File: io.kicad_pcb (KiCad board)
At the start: 2 copper layers, 182 x 139 mm, 37 parts, among them CON1 AVR_ISP, IC1 ATMEGA644P-P, J1 DB9, J2 DB9, P1 CONN_CTL_DATA, P2 CONN_ADDR, P3 SLOT1, P4 SLOT2, P5 SLOT3, P6 SLOT4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

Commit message: ugh
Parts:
- moved R2 18.3 mm to (115.7, 146.1)
- moved C11 7.62 mm to (70.0, 45.2)
- moved C12 7.62 mm to (51.3, 56.6)
- moved C9 7.62 mm to (51.3, 49.5)
- moved C10 7.62 mm to (70.0, 38.5)
- moved C8 7.62 mm to (51.3, 42.3)
- moved J2 7.62 mm to (95.6, 50.8)
- moved U6 7.62 mm to (57.1, 40.6)
- moved C2 6.60 mm to (150.8, 39.5)
- moved U1 6.60 mm to (158.8, 42.2)
- moved J1 3.81 mm to (84.7, 146.1)
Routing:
- net /A23: track 154.0 -> 219.4 mm
- net /RX: track 81.8 -> 41.2 mm
- net /TX: track 81.2 -> 41.6 mm
- net GND: track 513.9 -> 499.2 mm, vias 5 -> 4
- net /PAD_RIGHT: track 73.0 -> 59.4 mm
- net /PAD_SC: track 106.4 -> 94.2 mm
- net /A1: track 169.5 -> 181.5 mm
- net /PAD_LEFT: track 77.0 -> 65.3 mm
- net /A5: track 161.5 -> 173.1 mm
- net /PAD_AB: track 95.0 -> 85.3 mm
- net /PAD_DN: track 80.7 -> 71.0 mm
- net /A2: track 168.5 -> 177.5 mm
- net /~EN_S2: track 42.0 -> 33.2 mm
- net /A3: track 174.4 -> 183.1 mm
- net /A4: track 174.2 -> 182.5 mm
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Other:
- board size 182 x 139 mm -> 182 x 129 mm

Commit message: new layout
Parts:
- removed JP5: INT_S4, Pin_Headers:Pin_Header_Straight_2x01
- added R10: 4.7k, Resistors_SMD:R_0805, F.Cu at (20.8, 146.1)
- added R4: 4.7k, Resistors_SMD:R_0805, F.Cu at (20.8, 153.7)
- added R5: 4.7k, Resistors_SMD:R_0805, F.Cu at (37.1, 151.1)
- added R6: 4.7k, Resistors_SMD:R_0805, F.Cu at (20.8, 151.1)
- added R7: 4.7k, Resistors_SMD:R_0805, F.Cu at (37.0, 148.6)
- added R8: 4.7k, Resistors_SMD:R_0805, F.Cu at (20.8, 148.6)
- added R9: 4.7k, Resistors_SMD:R_0805, F.Cu at (37.0, 146.2)
- P6: value SLOT4 -> CONN_01X02; footprint m68kcomp1:edgecon_2x20 -> Pin_Headers:Pin_Header_Straight_1x02
- R1: moved to F.Cu
- R3: moved to B.Cu
- moved C2 221.0 mm to (-15.7, 184.7)
- moved C3 145.9 mm to (-5.00, 176.8)
- moved U1 130.6 mm to (38.1, 92.1), turned to 0 degrees
- moved P5 95.3 mm to (72.4, 73.7), turned to 90 degrees
- moved C4 91.1 mm to (36.4, 99.7), turned to 180 degrees
- moved U3 81.7 mm to (129.5, 160.0)
- moved C10 81.1 mm to (136.1, 85.5)
- moved C11 81.1 mm to (136.1, 92.2)
- moved C12 81.1 mm to (117.3, 103.6)
- moved C8 81.1 mm to (117.3, 89.3)
- moved C9 81.1 mm to (117.3, 96.5)
- moved U6 81.1 mm to (123.2, 87.6)
- moved P7 80.8 mm to (127.0, 73.7), turned to 90 degrees
- moved P4 80.8 mm to (72.4, 88.9), turned to 90 degrees
- moved IC1 79.5 mm to (50.8, 134.6), turned to 90 degrees
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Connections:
- net Net-(J2-Pad2) renamed /RS232_TX
- net Net-(J2-Pad3) renamed /RS232_RX
- J2 pad 7: (no net) -> /RS232_RTS
- J2 pad 8: (no net) -> /RS232_CTS
- P6 pad 1: VCC -> /RTS
- P6 pad 2: VCC -> /CTS
- U1 pad 11: /~EN_S4 -> (no net)
- U5 pad 10: /~DTACK -> (no net)
- U5 pad 11: Net-(P6-Pad9) -> GND
- U6 pad 10: (no net) -> /CTS
- U6 pad 7: (no net) -> /RS232_CTS
- U6 pad 8: (no net) -> /RS232_RTS
- U6 pad 9: (no net) -> /RTS
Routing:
- net /A8: track 448.4 -> 94.9 mm, vias 3 -> 2
- net /A10: track 435.6 -> 105.1 mm, vias 1 -> 2
- net /A9: track 437.3 -> 126.0 mm
- net /~AS: track 268.6 -> 32.6 mm, vias 1 -> 0
- net VCC: track 76.7 -> 303.9 mm, vias 0 -> 4
- net GND: track 499.2 -> 273.1 mm, vias 4 -> 6
- net /A12: track 310.4 -> 100.7 mm, vias 0 -> 2
- net /A11: track 313.4 -> 115.1 mm
- net /A14: track 298.6 -> 105.9 mm, vias 0 -> 2
- net /A13: track 301.3 -> 124.0 mm
- net /A16: track 286.6 -> 112.2 mm, vias 0 -> 2
- net /~IRQ6: track 168.2 -> 8.18 mm, vias 0 -> 1
- net /A15: track 289.3 -> 132.9 mm
- net /A18: track 274.5 -> 118.2 mm, vias 0 -> 2
- net /~WR: track 259.4 -> 107.2 mm, vias 2 -> 1
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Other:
- board size 182 x 129 mm -> 142 x 100 mm

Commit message: layout progresses
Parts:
- moved C2 167.5 mm to (136.9, 115.7)
- moved C3 122.6 mm to (103.0, 118.8), turned to 270 degrees
- moved U5 9.84 mm to (135.1, 121.8), turned to 0 degrees
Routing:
- net /~DTACK: track 0.00 -> 182.8 mm, vias 0 -> 3
- net Net-(P5-Pad9): track 0.00 -> 163.3 mm
- net Net-(P4-Pad9): track 0.00 -> 108.9 mm
- net Net-(P3-Pad9): track 0.00 -> 83.1 mm
- net /~IRQ5: track 141.1 -> 215.1 mm
- net /DTACK: track 0.00 -> 48.5 mm, vias 0 -> 1
- net /~INTS3: track 0.00 -> 47.9 mm
- net /~INTS2: track 0.00 -> 39.5 mm, vias 0 -> 2
- net /~INTS1: track 0.00 -> 36.6 mm, vias 0 -> 2
- net /~IRQ3: track 143.1 -> 127.8 mm
- net /~IRQ4: track 137.0 -> 123.2 mm
- net GND: track 273.1 -> 278.5 mm
- net VCC: track 303.9 -> 308.7 mm

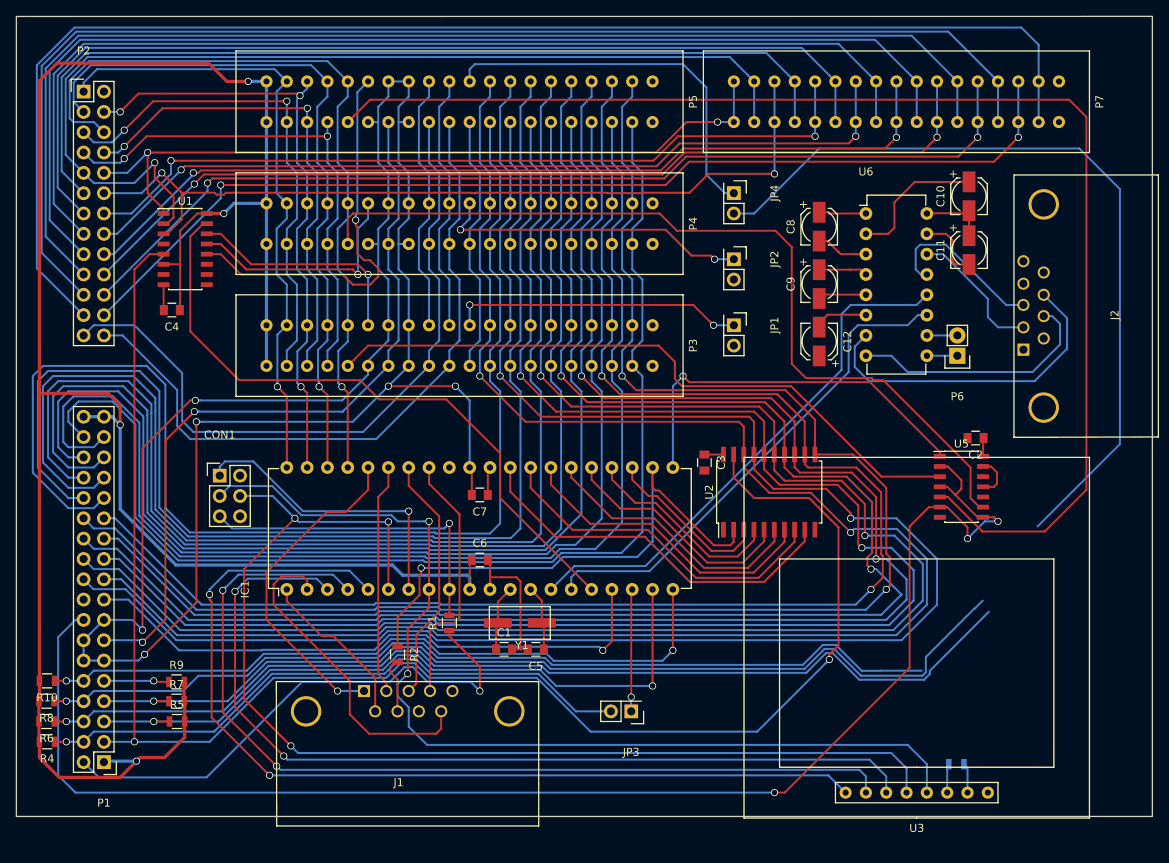
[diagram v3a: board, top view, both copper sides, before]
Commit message: I/O PCB almost done
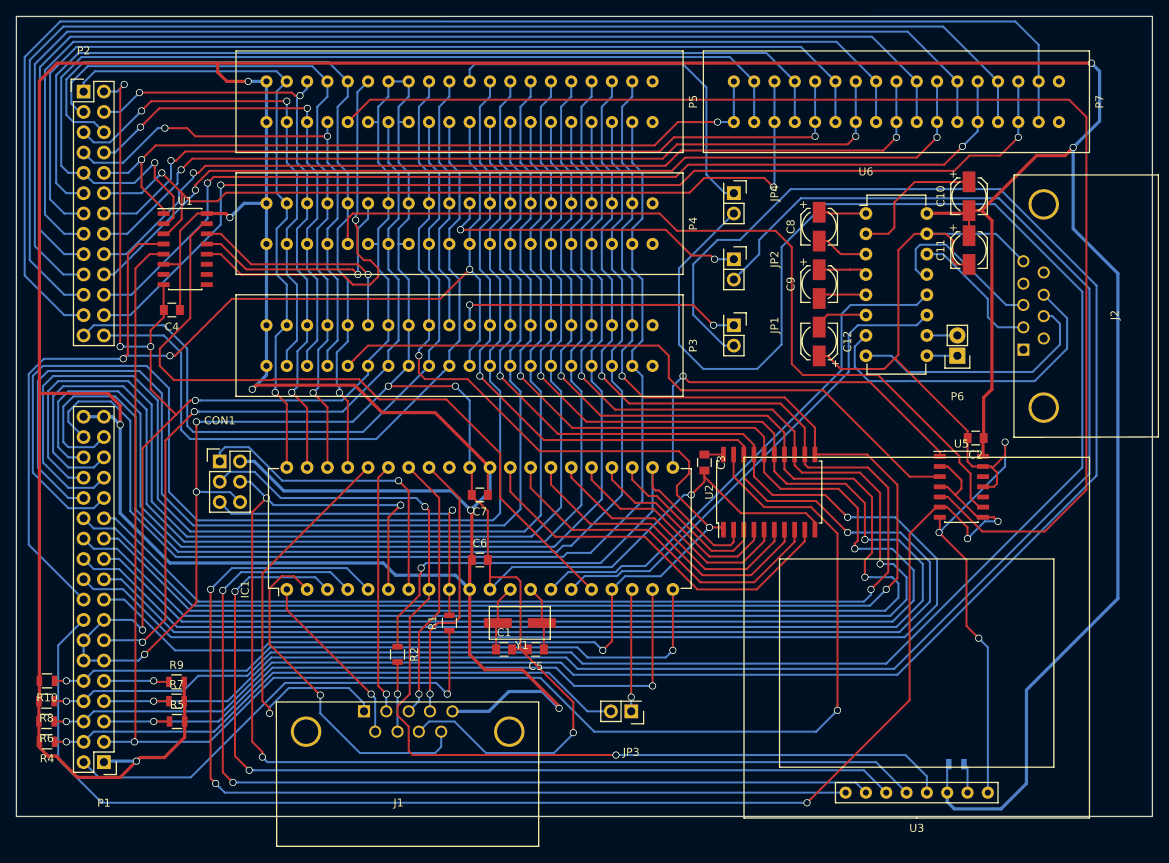
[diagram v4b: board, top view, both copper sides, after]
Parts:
- moved J1 2.54 mm to (60.5, 149.9)
- moved CON1 1.78 mm to (42.4, 118.6)
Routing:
- net VCC: track 308.7 -> 694.4 mm, vias 4 -> 9
- net GND: track 278.5 -> 551.7 mm, vias 6 -> 15
- net /~IRQ3: track 127.8 -> 240.3 mm
- net /~AS: track 32.6 -> 142.6 mm, vias 0 -> 3
- net /~IRQ4: track 123.2 -> 215.6 mm
- net /~WR: track 107.2 -> 179.2 mm, vias 1 -> 3
- net /~IRQ5: track 215.1 -> 254.9 mm
- net /PAD_UP: track 41.6 -> 51.9 mm
- net /~EN_AVR: track 81.4 -> 89.4 mm
- net /~SYS_RESET: track 99.0 -> 92.4 mm
- net /MOSI: track 143.0 -> 148.5 mm
- net /A23: track 171.4 -> 176.2 mm
- net /DM_RST: track 121.0 -> 125.6 mm
- net /A21: track 159.7 -> 164.2 mm
- net /A19: track 150.8 -> 155.0 mm
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
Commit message: mostly done
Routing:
- net VCC: track 694.4 -> 779.2 mm, vias 9 -> 12
- net /~SYS_RESET: track 92.4 -> 152.5 mm, vias 1 -> 3
- net GND: track 551.7 -> 575.1 mm, vias 15 -> 16
- net /~LDS: track 90.6 -> 94.2 mm
- net /~IRQ5: track 254.9 -> 256.8 mm
- net /DTACK: track 48.5 -> 50.4 mm
- net /~IRQ4: track 215.6 -> 217.4 mm
- net /~IRQ3: track 240.3 -> 242.0 mm
- net /A18: track 118.8 -> 120.0 mm

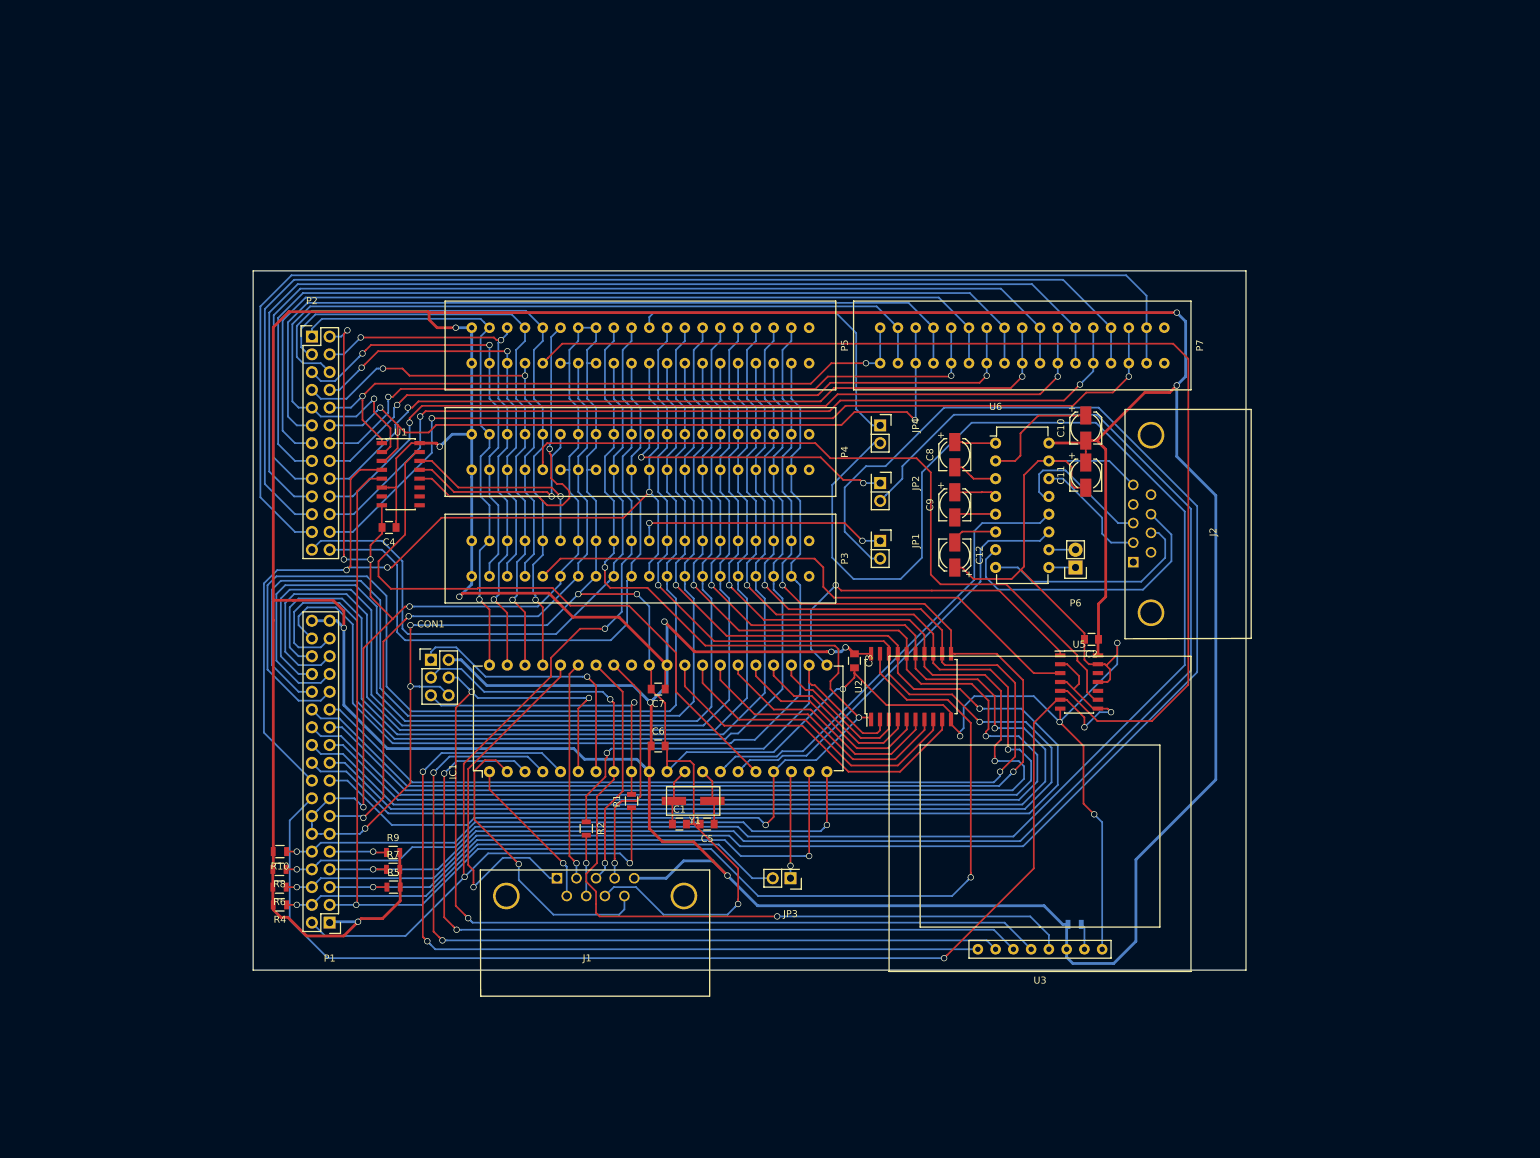
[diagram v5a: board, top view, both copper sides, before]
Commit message: increased the via pad size
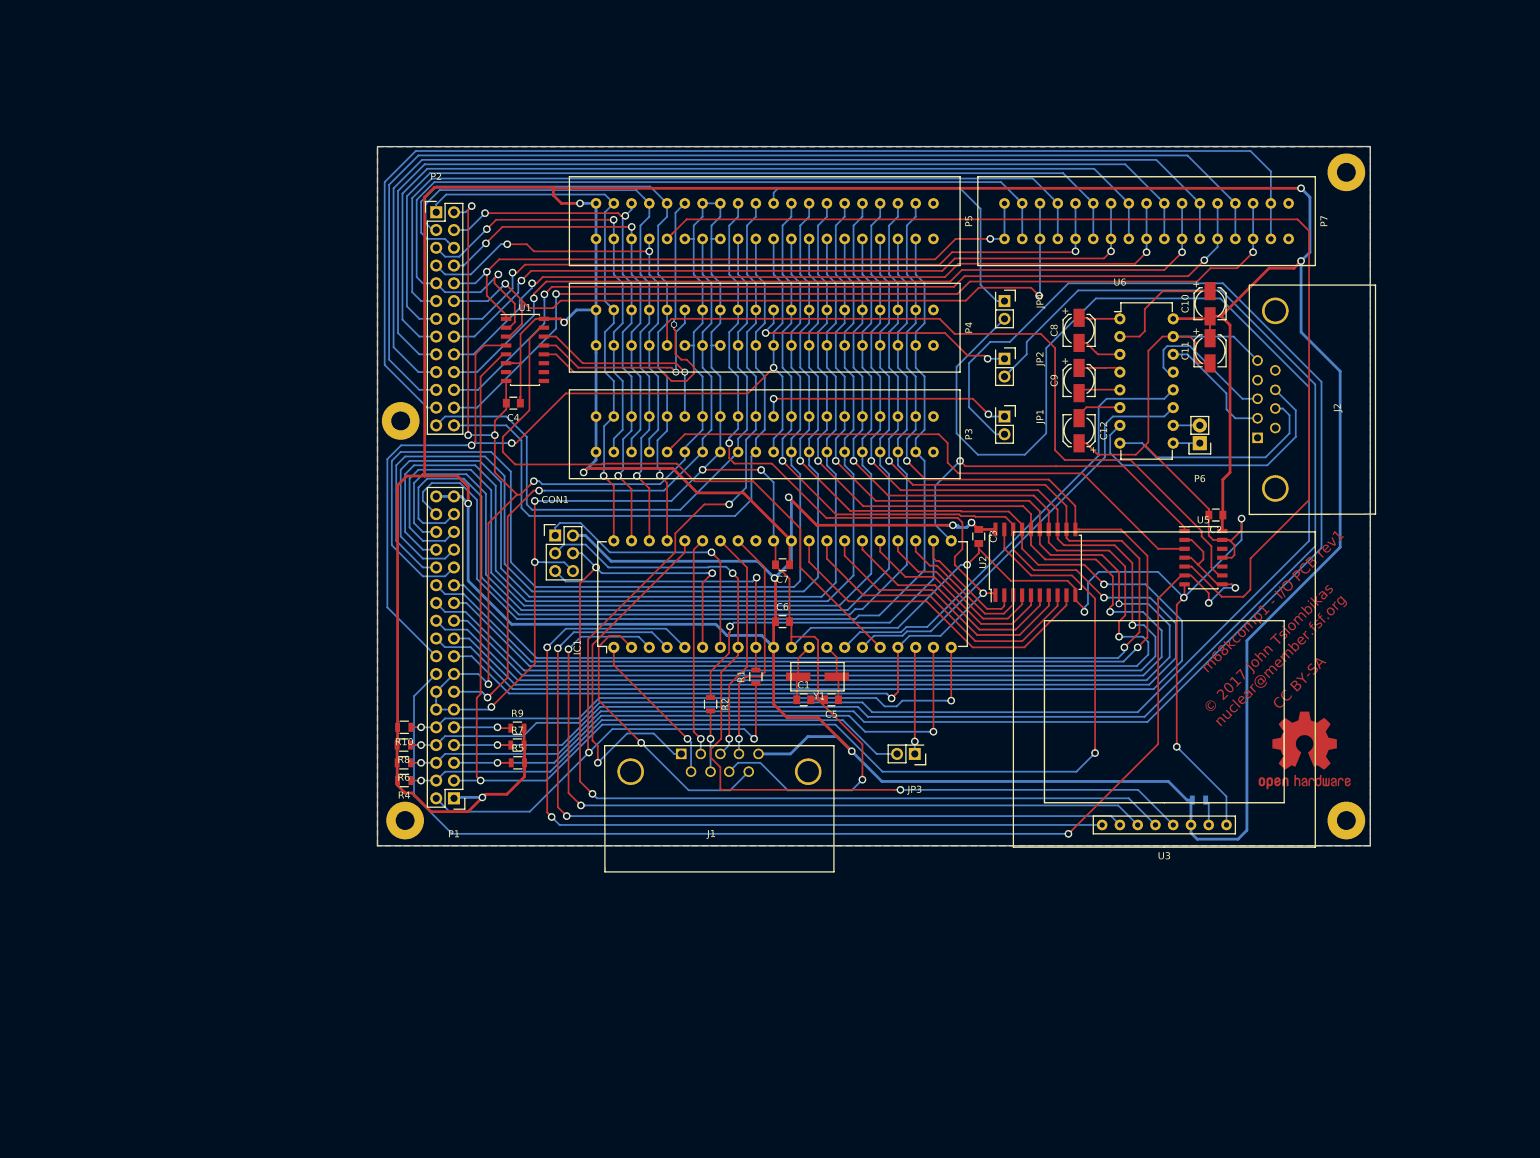
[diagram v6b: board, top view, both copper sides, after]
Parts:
- added REF**: MountingHole_2.7mm_M2.5_Pad, Mounting_Holes:MountingHole_2.7mm_M2.5_Pad, F.Cu at (173.4, 48.9)
- added REF**: MountingHole_2.7mm_M2.5_Pad, Mounting_Holes:MountingHole_2.7mm_M2.5_Pad, F.Cu at (38.7, 141.6)
- added REF**: MountingHole_2.7mm_M2.5_Pad, Mounting_Holes:MountingHole_2.7mm_M2.5_Pad, F.Cu at (173.4, 141.6)
- added REF**: MountingHole_2.7mm_M2.5_Pad, Mounting_Holes:MountingHole_2.7mm_M2.5_Pad, F.Cu at (38.1, 84.5)
- added REF***: OSHW-Logo2_14.6x12mm_Copper, Symbols:OSHW-Logo2_14.6x12mm_Copper, F.Cu at (167.4, 131.6)
- moved U2 25.1 mm to (128.9, 104.7)
- moved C1 25.1 mm to (95.7, 124.3)
- moved C10 25.1 mm to (153.9, 67.7)
- moved C11 25.1 mm to (153.9, 74.4)
- moved C2 25.1 mm to (154.7, 97.9)
- moved C3 25.1 mm to (120.8, 101.0)
- moved C5 25.1 mm to (99.7, 124.3)
- moved C6 25.1 mm to (92.7, 113.2)
- moved CON1 25.1 mm to (60.2, 100.8)
- moved IC1 25.1 mm to (68.6, 116.8)
- moved J1 25.1 mm to (78.2, 132.1)
- moved J2 25.1 mm to (160.7, 86.9)
- moved JP3 25.1 mm to (111.6, 132.1)
- moved P2 25.1 mm to (43.2, 54.6)
- moved P3 25.1 mm to (90.2, 86.4)
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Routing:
- net VCC: track 779.2 -> 775.2 mm
- net Net-(P5-Pad9): track 163.3 -> 160.1 mm
- net /PAD_SC: track 43.6 -> 41.6 mm
- net GND: track 575.1 -> 577.0 mm
- net /SCK: track 129.0 -> 127.9 mm
- net /~WR: track 179.6 -> 178.5 mm
- net /CLK20: track 95.7 -> 96.5 mm
- net /A23: track 176.2 -> 175.5 mm
- net /~IRQ5: track 256.8 -> 256.3 mm
- added copper zone on B.Cu, net GND
- added copper zone on F.Cu, net GND
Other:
- net class Default: via_dia 0.9 -> 1.1
- board text added: "CC BY-SA"
- board text added: "m68kcomp1 - I/O PCB rev1"
- board text added: "© 2017 John Tsiombikas nuclear@member.fsf.org"

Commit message: io lite
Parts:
- removed JP4: INT_S3, Pin_Headers:Pin_Header_Straight_2x01
- removed REF** (x4): MountingHole_2.7mm_M2.5_Pad, Mounting_Holes:MountingHole_2.7mm_M2.5_Pad
- P3: value SLOT1 -> SLOT_PWR; footprint m68kcomp1:edgecon_2x20 -> Pin_Headers:Pin_Header_Angled_1x03
- P4: value SLOT2 -> SLOT1; footprint m68kcomp1:edgecon_2x20 -> m68kcomp1:edgecon_2x17
- P5: value SLOT3 -> SLOT2; footprint m68kcomp1:edgecon_2x20 -> m68kcomp1:edgecon_2x17
- moved P3 87.3 mm to (172.6, 57.6), turned to 0 degrees
- moved P4 10.6 mm to (90.7, 81.7)
- moved J2 9.02 mm to (161.8, 95.8)
- moved REF*** 6.51 mm to (168.5, 138.0)
- moved P7 4.32 mm to (144.0, 60.1)
- moved P5 4.28 mm to (90.7, 60.1)
- moved R10 3.81 mm to (38.6, 124.5)
- moved C1 3.81 mm to (95.7, 120.5)
- moved C5 3.81 mm to (99.7, 120.5)
- moved C6 3.81 mm to (92.7, 109.3)
- moved C7 3.81 mm to (92.7, 101.2)
- moved IC1 3.81 mm to (68.6, 113.0)
- moved JP2 3.81 mm to (124.5, 71.8)
- moved JP3 3.81 mm to (111.6, 128.3)
- moved P1 3.81 mm to (45.7, 134.6)
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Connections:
- P3 pad 2: VCC -> GND
- P3 pad 3: /A5 -> GND
- P4 pad 1: VCC -> /A4
- P4 pad 10: /A4 -> /~EN_S1
- P4 pad 11: GND -> /CLK20
- P4 pad 12: /~EN_S2 -> VCC
- P4 pad 13: /CLK20 -> /~UDS
- P4 pad 14: GND -> /~WR
- P4 pad 15: GND -> /~LDS
- P4 pad 16: GND -> /~SYS_RESET
- P4 pad 17: /~UDS -> /~AS
- P4 pad 18: /~WR -> /~INTS1
- P4 pad 19: /~LDS -> /BUS8
- P4 pad 2: VCC -> /A1
- P4 pad 20: /~SYS_RESET -> /BUS0
- P4 pad 21: /~AS -> /BUS9
- P4 pad 22: /~INTS2 -> /BUS1
- P4 pad 23: /BUS8 -> /BUS10
- P4 pad 24: /BUS0 -> /BUS2
- P4 pad 25: /BUS9 -> /BUS11
- P4 pad 26: /BUS1 -> /BUS3
- P4 pad 27: /BUS10 -> /BUS12
- P4 pad 28: /BUS2 -> /BUS4
- P4 pad 29: /BUS11 -> /BUS13
- P4 pad 30: /BUS3 -> /BUS5
- P4 pad 31: /BUS12 -> /BUS14
- P4 pad 32: /BUS4 -> /BUS6
- P4 pad 33: /BUS13 -> /BUS15
- P4 pad 34: /BUS5 -> /BUS7
- P4 pad 4: /A1 -> /A2
- P4 pad 6: /A2 -> /A3
- P4 pad 8: /A3 -> GND
- P4 pad 9: Net-(P4-Pad9) -> /DTACK_S1
- P5 pad 1: VCC -> /A4
- P5 pad 10: /A4 -> /~EN_S2
- P5 pad 11: GND -> /CLK20
- P5 pad 12: /~EN_S3 -> VCC
- P5 pad 13: /CLK20 -> /~UDS
- P5 pad 14: GND -> /~WR
- P5 pad 15: GND -> /~LDS
- P5 pad 16: GND -> /~SYS_RESET
- P5 pad 17: /~UDS -> /~AS
- P5 pad 18: /~WR -> /~INTS2
- P5 pad 19: /~LDS -> /BUS8
- P5 pad 2: VCC -> /A1
- P5 pad 20: /~SYS_RESET -> /BUS0
- P5 pad 21: /~AS -> /BUS9
- P5 pad 22: /~INTS3 -> /BUS1
- P5 pad 23: /BUS8 -> /BUS10
- P5 pad 24: /BUS0 -> /BUS2
- P5 pad 25: /BUS9 -> /BUS11
- P5 pad 26: /BUS1 -> /BUS3
- P5 pad 27: /BUS10 -> /BUS12
- P5 pad 28: /BUS2 -> /BUS4
- P5 pad 29: /BUS11 -> /BUS13
- P5 pad 30: /BUS3 -> /BUS5
- P5 pad 31: /BUS12 -> /BUS14
- P5 pad 32: /BUS4 -> /BUS6
- P5 pad 33: /BUS13 -> /BUS15
- P5 pad 34: /BUS5 -> /BUS7
- P5 pad 4: /A1 -> /A2
- P5 pad 6: /A2 -> /A3
- P5 pad 8: /A3 -> GND
- P5 pad 9: Net-(P5-Pad9) -> /DTACK_S2
- P7 pad 33: (no net) -> VCC
- P7 pad 34: (no net) -> GND
- U1 pad 12: /~EN_S3 -> (no net)
- U5 pad 3: Net-(P3-Pad9) -> /DTACK_S1
- U5 pad 5: Net-(P5-Pad9) -> (no net)
- U5 pad 6: /~DTACK -> (no net)
- U5 pad 9: Net-(P4-Pad9) -> /DTACK_S2
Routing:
- net /~IRQ5: track 256.3 -> 3.69 mm
- net GND: track 577.0 -> 388.4 mm, vias 16 -> 11
- net Net-(P5-Pad9): track 160.1 -> 0.00 mm
- net /DTACK_S2: track 0.00 -> 119.4 mm, vias 0 -> 1
- net Net-(P4-Pad9): track 108.9 -> 0.00 mm
- net Net-(P3-Pad9): track 83.5 -> 0.00 mm
- net /DTACK_S1: track 0.00 -> 78.3 mm, vias 0 -> 1
- net /SCK: track 127.9 -> 187.3 mm, vias 2 -> 3
- net /~EN_S3: track 50.1 -> 0.00 mm, vias 1 -> 0
- net /~INTS3: track 47.9 -> 0.00 mm
- net /~LDS: track 94.2 -> 69.9 mm, vias 0 -> 2
- net /~UDS: track 90.9 -> 70.7 mm, vias 0 -> 2
- net /A4: track 98.6 -> 82.1 mm, vias 1 -> 2
- net /~EN_S2: track 29.9 -> 45.9 mm
- net /BUS8: track 149.7 -> 137.6 mm
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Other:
- board text added: "m68kcomp1 - I/O PCB rev2"
- board text removed: "m68kcomp1 - I/O PCB rev1"
